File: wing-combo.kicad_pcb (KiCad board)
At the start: 2 copper layers, 93 x 91.3 mm, 114 parts, among them J1 Screw_Terminal_01x06, J13 USB_A, J15 Conn_01x16, J16 Conn_01x16, J17 Screw_Terminal_01x06, J18 Screw_Terminal_01x06, J3 Conn_01x12, J4 Conn_01x12, T1 AO3400A, T2 AO3400A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

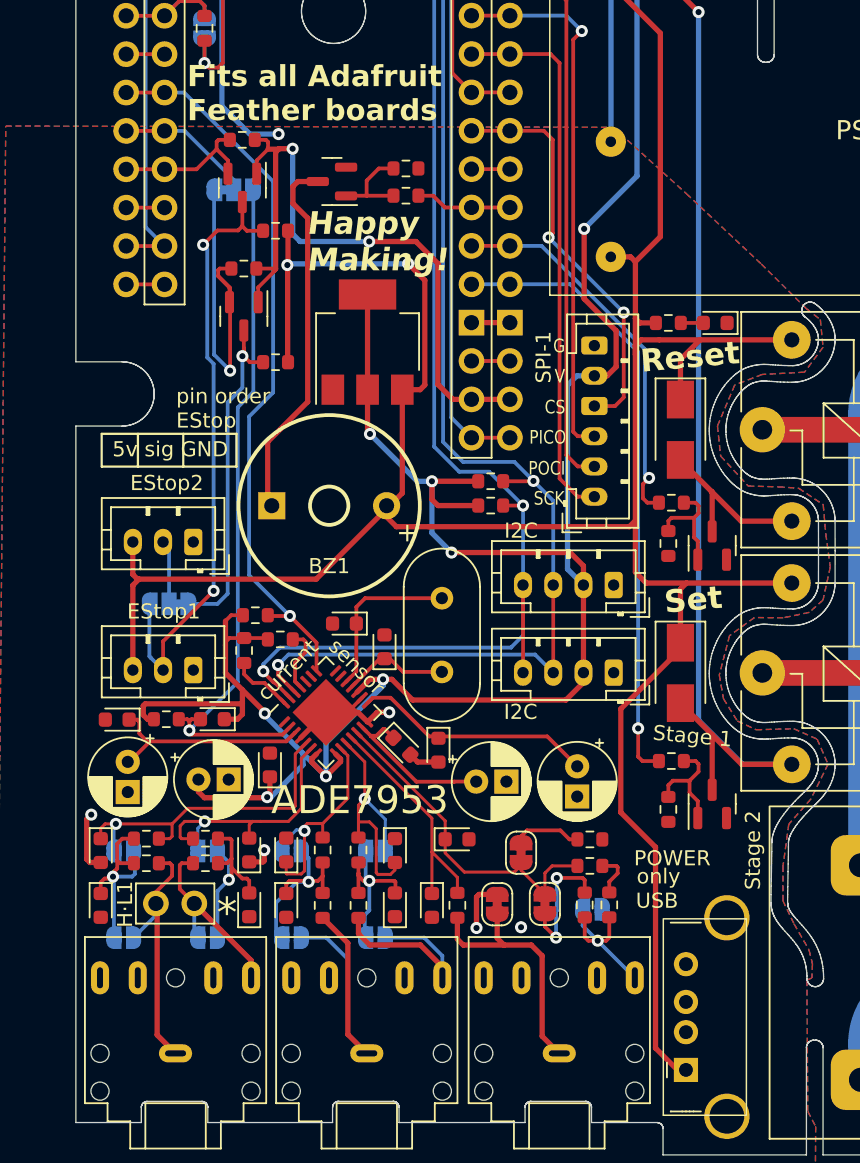
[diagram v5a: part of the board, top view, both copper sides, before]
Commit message: added USBC for power. Changed Feather power-supply to be incompliance with Feather's recommendations
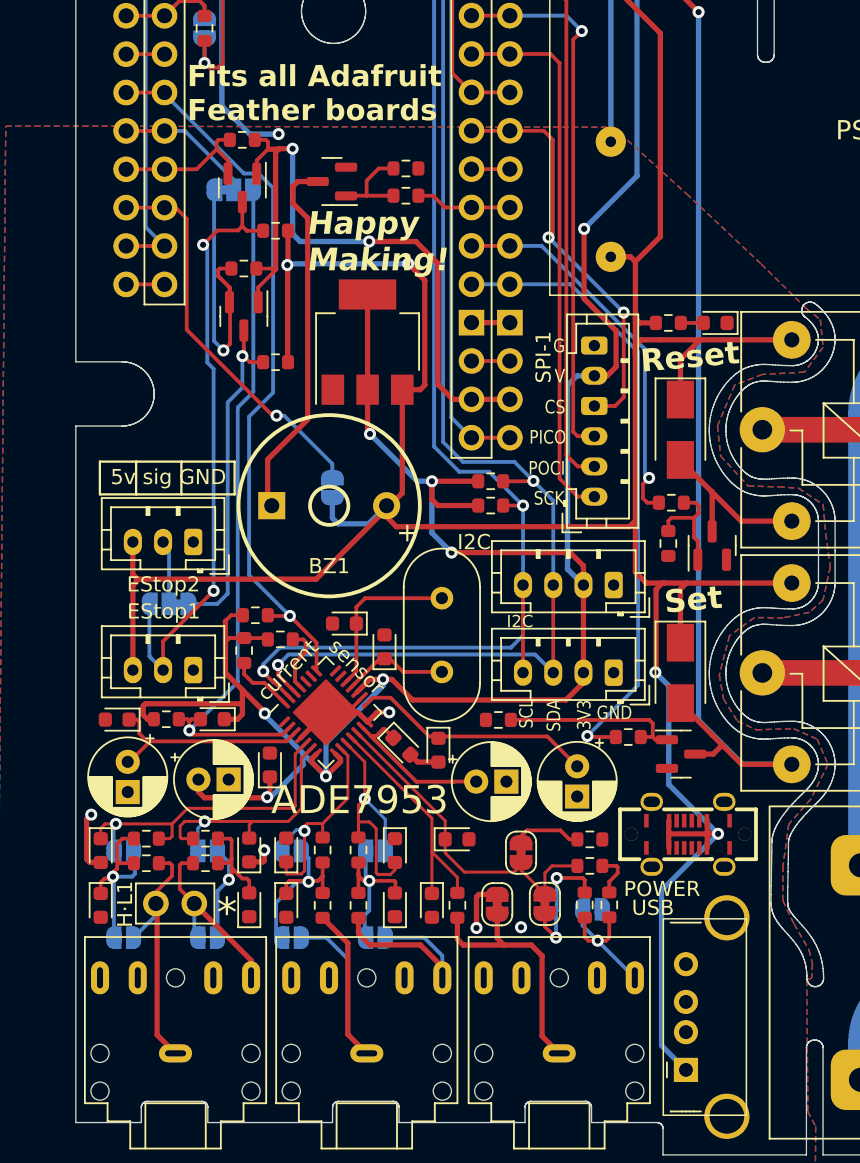
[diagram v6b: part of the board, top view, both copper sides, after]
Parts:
- added J5: USB_C_Receptacle_USB2.0_16P, usbc:USB-C-TH_GT-USB-7055, F.Cu at (77.4, 93.0)
- added JP17: no-filter-1, Jumper:SolderJumper-2_P1.3mm_Open_RoundedPad1.0x1.5mm, B.Cu at (53.9, 70.0)
- moved R28 12.7 mm to (64.9, 85.4), turned to 180 degrees
- moved T3 3.89 mm to (77.0, 87.6), turned to 0 degrees
- moved R27 3.26 mm to (73.5, 86.5)
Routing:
- net Net-(J3-Pin_10): track 2.54 -> 25.9 mm, vias 0 -> 1
- net +5V: track 191.5 -> 208.9 mm, vias 2 -> 4
- net Net-(T3-G): track 7.41 -> 12.2 mm
- net read-aux-E-Stop: track 22.3 -> 19.7 mm
- net Net-(D3-A): track 75.5 -> 74.0 mm
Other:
- board text added: "3V3"
- board text added: "SCL"
- board text added: "SDA"
- board text removed: "Stage 1"
- board text removed: "Stage 2"
- board text removed: "only"
- board text removed: "pin order EStop"
